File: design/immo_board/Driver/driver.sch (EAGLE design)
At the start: 24 parts, among them IC2 LM393N, IC3 74LS241N

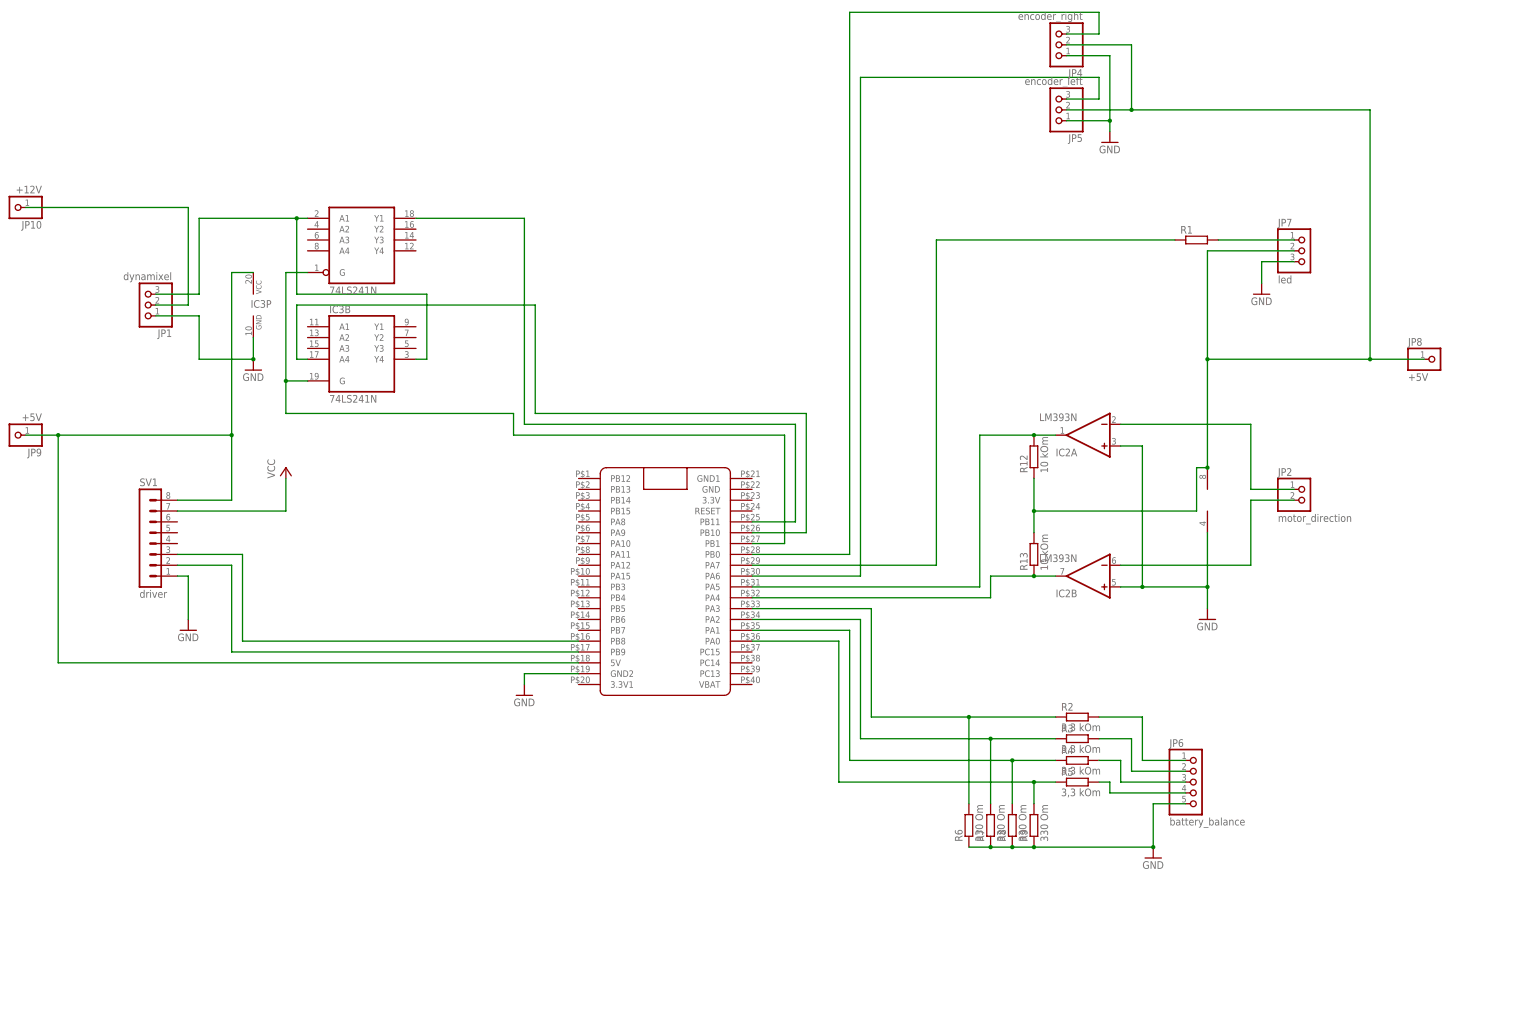
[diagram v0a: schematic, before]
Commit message: Add board for driver. Fix electric scheme.
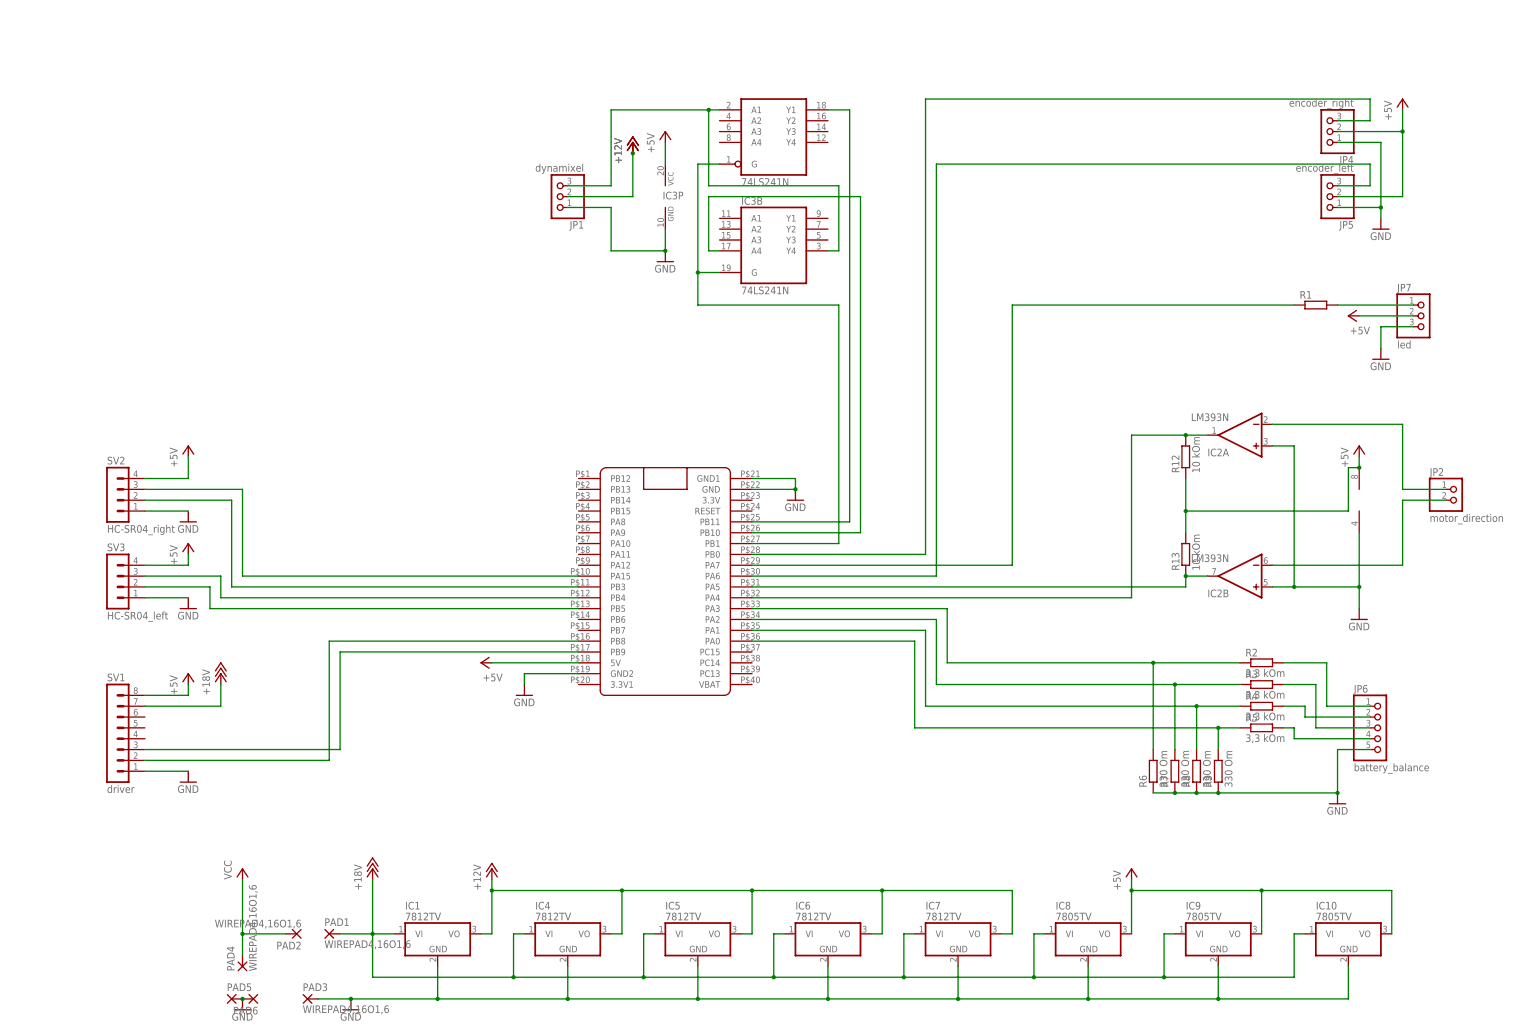
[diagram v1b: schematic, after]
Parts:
- removed JP10: +12V, pinhead:PINHD-1X1
- removed JP8, JP9: +5V, pinhead:PINHD-1X1
- added IC1, IC4, IC5, IC6, IC7: 7812TV, linear:7812TV
- added IC10, IC8, IC9: 7805TV, linear:7805TV
- added PAD1, PAD2, PAD3, PAD4: WIREPAD4,16O1,6, wirepad:WIREPAD4,16O1,6
- added PAD5, PAD6: (no value), wirepad:2,54/1,0
- added SV2: HC-SR04_right, con-lstb:MA04-1
- added SV3: HC-SR04_left, con-lstb:MA04-1
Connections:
- removed net N$24: JP1.2, JP10.1
- new net +12V: IC1.VO, IC4.VO, IC5.VO, IC6.VO, IC7.VO, JP1.2
- new net +18V: IC1.VI, IC10.VI, IC4.VI, IC5.VI, IC6.VI, IC7.VI, IC8.VI, IC9.VI, PAD1.P, SV1.7
- new net +5V: IC10.VO, IC2P.V+, IC3P.VCC, IC8.VO, IC9.VO, JP4.2, JP5.2, JP7.2, R12.1, R13.2, SV1.8, SV2.4, SV3.4, U$1.5V
- new net N$28: SV2.3, U$1.PA15
- new net N$29: SV2.2, U$1.PB3
- net GND: now also IC1.GND, IC10.GND, IC4.GND, IC5.GND, IC6.GND, IC7.GND, IC8.GND, IC9.GND, PAD3.P, PAD5.P, PAD6.P, SV2.1, SV3.1, U$1.GND, U$1.GND1
- net N$14: now also U$1.PA5; no longer U$1.PA4
- net N$20: now also SV1.3; no longer SV1.2
- net N$21: now also SV1.2; no longer SV1.3
- net N$23: now also SV3.2, U$1.PB5; no longer IC2P.V+, JP4.2, JP5.2, JP7.2, JP8.1, R12.1, R13.2
- net N$25: now also SV3.3, U$1.PB4; no longer IC3P.VCC, JP9.1, SV1.8, U$1.5V
- net N$6: now also JP6.2; no longer JP6.3
- net N$7: now also JP6.3; no longer JP6.2
- net N$9: now also U$1.PA4; no longer U$1.PA5
- net VCC: now also PAD2.P, PAD4.P; no longer SV1.7
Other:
- moved on the sheet: IC2A, IC2B, IC3B, IC3P, JP1, JP2, JP4, JP5, JP6, JP7, R1, R12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

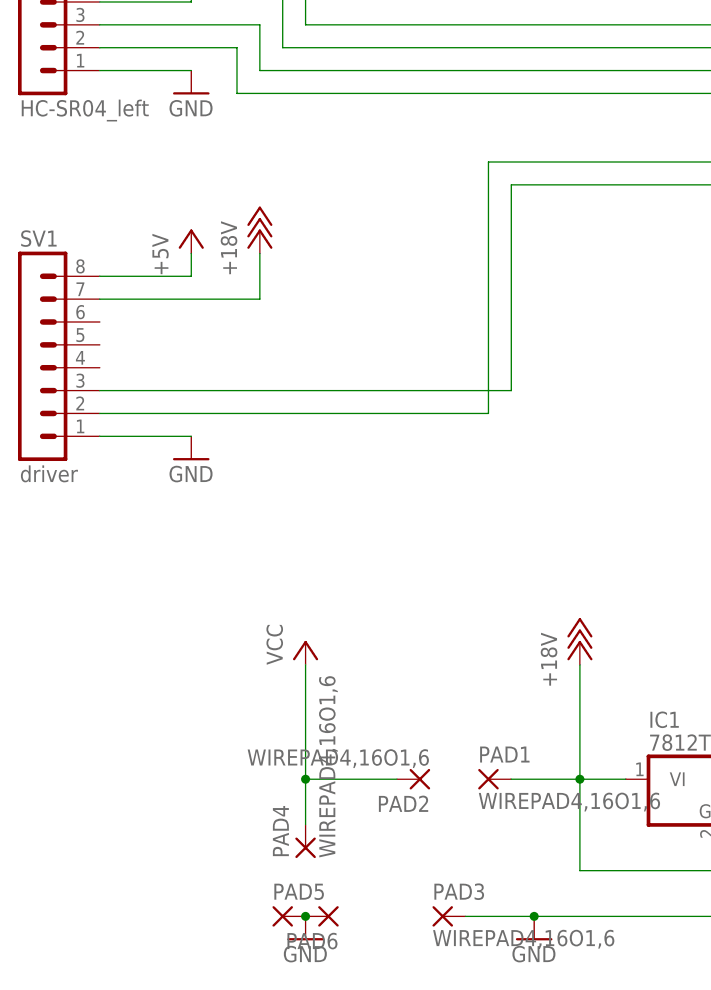
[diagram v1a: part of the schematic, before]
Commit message: Fix board for driver. Fix electric scheme.
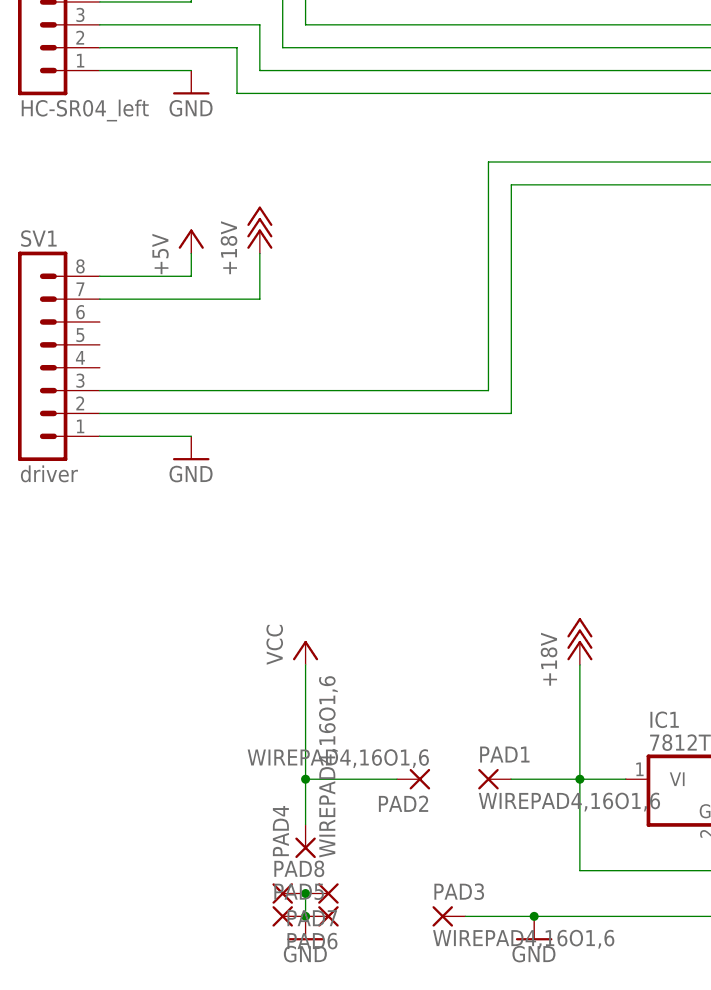
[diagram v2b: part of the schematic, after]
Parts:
- added PAD7, PAD8: (no value), wirepad:2,54/1,0
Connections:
- net GND: now also PAD7.P, PAD8.P
- net N$20: now also SV1.2; no longer SV1.3
- net N$21: now also SV1.3; no longer SV1.2
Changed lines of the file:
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@@
 <part name="PAD6" library="wirepad" deviceset="2,54/1,0" device=""/>
 <part name="GND12" library="supply1" deviceset="GND" device=""/>
+<part name="PAD7" library="wirepad" deviceset="2,54/1,0" device=""/>
+<part name="PAD8" library="wirepad" deviceset="2,54/1,0" device=""/>
 </parts>
 <sheets>
@@
 <instance part="PAD6" gate="P" x="5.08" y="-91.44" rot="R180"/>
 <instance part="GND12" gate="1" x="2.54" y="-93.98"/>
+<instance part="PAD7" gate="P" x="5.08" y="-88.9" rot="R180"/>
+<instance part="PAD8" gate="P" x="0" y="-88.9"/>
 </instances>
 <busses>
@@
 <pinref part="GND12" gate="1" pin="GND"/>
 <junction x="2.54" y="-91.44"/>
-<pinref part="GND12" gate="1" pin="GND"/>
+<pinref part="PAD7" gate="P" pin="P"/>
+<pinref part="PAD8" gate="P" pin="P"/>
+<wire x1="2.54" y1="-91.44" x2="2.54" y2="-88.9" width="0.1524" layer="91"/>
+<junction x="2.54" y="-88.9"/>
 </segment>
 </net>
@@
 <pinref part="U$1" gate="G$1" pin="PB9"/>
 <wire x1="25.4" y1="-10.16" x2="81.28" y2="-10.16" width="0.1524" layer="91"/>
-<wire x1="25.4" y1="-10.16" x2="25.4" y2="-33.02" width="0.1524" layer="91"/>
-<pinref part="SV1" gate="1" pin="3"/>
-<wire x1="25.4" y1="-33.02" x2="-20.32" y2="-33.02" width="0.1524" layer="91"/>
+<wire x1="25.4" y1="-10.16" x2="25.4" y2="-35.56" width="0.1524" layer="91"/>
+<pinref part="SV1" gate="1" pin="2"/>
+<wire x1="-20.32" y1="-35.56" x2="25.4" y2="-35.56" width="0.1524" layer="91"/>
 </segment>
 </net>
@@
 <pinref part="U$1" gate="G$1" pin="PB8"/>
 <wire x1="81.28" y1="-7.62" x2="22.86" y2="-7.62" width="0.1524" layer="91"/>
-<wire x1="22.86" y1="-7.62" x2="22.86" y2="-35.56" width="0.1524" layer="91"/>
-<pinref part="SV1" gate="1" pin="2"/>
-<wire x1="-20.32" y1="-35.56" x2="22.86" y2="-35.56" width="0.1524" layer="91"/>
-</segment>
-</net>
+<wire x1="22.86" y1="-7.62" x2="22.86" y2="-33.02" width="0.1524" layer="91"/>
+<pinref part="SV1" gate="1" pin="3"/>
+<wire x1="22.86" y1="-33.02" x2="-20.32" y2="-33.02" width="0.1524" layer="91"/>
+</segment>
+</net>

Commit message: Fix board and electrical scheme for Encoder, Driver, WS2812B.
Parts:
- removed PAD5, PAD6, PAD7, PAD8: (no value), wirepad:2,54/1,0
- R1: value (none) -> 330 Om
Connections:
- net N$1 renamed P$27
- net N$10 renamed P$36
- net N$11 renamed P$35
- net N$12 renamed P$34
- net N$13 renamed P$33
- net N$14 renamed P$31
- net N$15 renamed P$30
- net N$18 renamed P$29
- net N$20 renamed P$17
- net N$21 renamed P$16
- net N$22 renamed P$28
- net N$23 renamed P$13
- net N$25 renamed P$12
- net N$28 renamed P$10
- net N$29 renamed P$11
- net N$3 renamed P$25
- net N$4 renamed P$26
- net N$9 renamed P$32
- net GND: no longer PAD5.P, PAD6.P, PAD7.P, PAD8.P

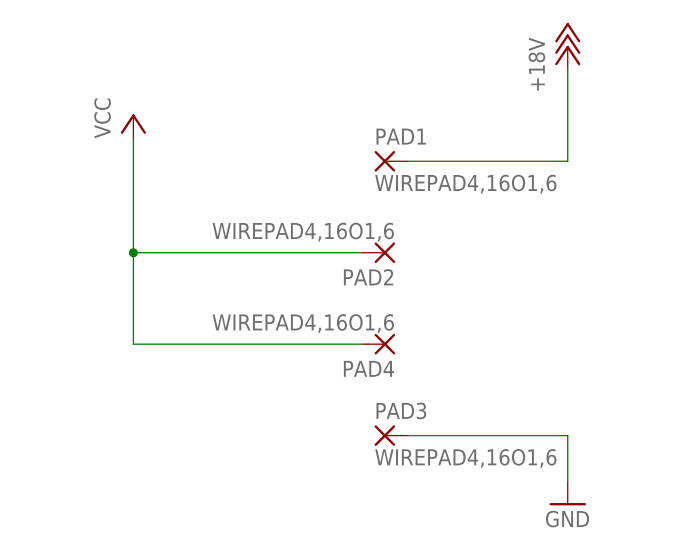
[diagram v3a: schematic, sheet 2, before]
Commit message: Fix board and electric scheme. Add capacitors.
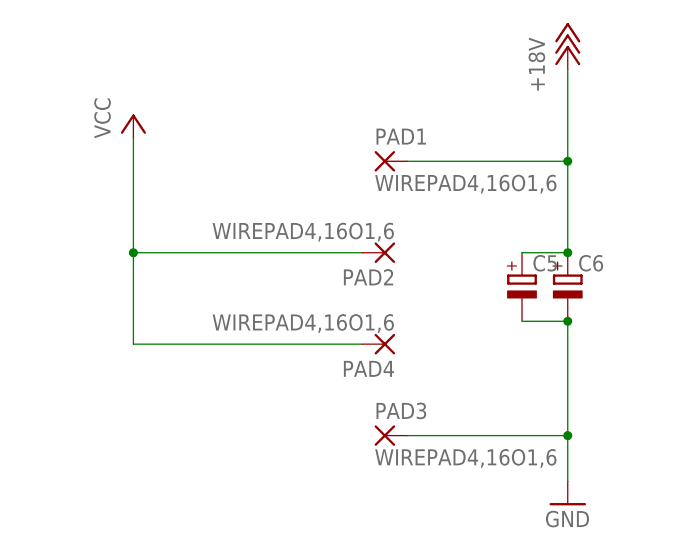
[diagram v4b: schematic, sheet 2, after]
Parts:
- added C1, C4, C5: (no value), resistor:CPOL-EUE5-8.5
- added C2, C3, C6: (no value), resistor:CPOL-EUE2.5-5
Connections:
- net +12V: now also C1.+, C2.+
- net +18V: now also C5.+, C6.+
- net +5V: now also C3.+, C4.+
- net GND: now also C1.-, C2.-, C3.-, C4.-, C5.-, C6.-
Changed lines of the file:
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@@
 <part name="P+17" library="supply1" deviceset="+18V" device=""/>
 <part name="GND14" library="supply1" deviceset="GND" device=""/>
+<part name="C1" library="resistor" deviceset="CPOL-EU" device="E5-8.5"/>
+<part name="C2" library="resistor" deviceset="CPOL-EU" device="E2.5-5"/>
+<part name="C3" library="resistor" deviceset="CPOL-EU" device="E2.5-5"/>
+<part name="C4" library="resistor" deviceset="CPOL-EU" device="E5-8.5"/>
+<part name="C5" library="resistor" deviceset="CPOL-EU" device="E5-8.5"/>
+<part name="C6" library="resistor" deviceset="CPOL-EU" device="E2.5-5"/>
 </parts>
 <sheets>
@@
 <instance part="P+17" gate="1" x="60.96" y="30.48"/>
 <instance part="GND14" gate="1" x="60.96" y="-20.32"/>
+<instance part="C5" gate="G$1" x="55.88" y="5.08"/>
+<instance part="C6" gate="G$1" x="60.96" y="5.08"/>
 </instances>
 <busses>
@@
 <pinref part="PAD3" gate="G$1" pin="P"/>
 <wire x1="43.18" y1="-12.7" x2="60.96" y2="-12.7" width="0.1524" layer="91"/>
+<pinref part="C6" gate="G$1" pin="-"/>
+<wire x1="60.96" y1="-12.7" x2="60.96" y2="0" width="0.1524" layer="91"/>
+<junction x="60.96" y="-12.7"/>
+<pinref part="C5" gate="G$1" pin="-"/>
+<wire x1="60.96" y1="0" x2="55.88" y2="0" width="0.1524" layer="91"/>
+<junction x="60.96" y="0"/>
 </segment>
 </net>
@@
 <wire x1="43.18" y1="17.78" x2="60.96" y2="17.78" width="0.1524" layer="91"/>
 <wire x1="60.96" y1="17.78" x2="60.96" y2="27.94" width="0.1524" layer="91"/>
+<pinref part="C5" gate="G$1" pin="+"/>
+<pinref part="C6" gate="G$1" pin="+"/>
+<wire x1="55.88" y1="7.62" x2="60.96" y2="7.62" width="0.1524" layer="91"/>
+<wire x1="60.96" y1="7.62" x2="60.96" y2="17.78" width="0.1524" layer="91"/>
+<junction x="60.96" y="7.62"/>
+<junction x="60.96" y="17.78"/>
 </segment>
 </net>
@@
 <instance part="P+4" gate="1" x="-10.16" y="71.12"/>
 <instance part="P+6" gate="1" x="17.78" y="71.12"/>
+<instance part="C1" gate="G$1" x="139.7" y="45.72"/>
+<instance part="C2" gate="G$1" x="134.62" y="45.72"/>
 </instances>
 <busses>
@@
 <junction x="96.52" y="40.64"/>
 <pinref part="GND8" gate="1" pin="GND"/>
+<pinref part="C2" gate="G$1" pin="-"/>
+<wire x1="127" y1="40.64" x2="134.62" y2="40.64" width="0.1524" layer="91"/>
+<junction x="127" y="40.64"/>
+<pinref part="C1" gate="G$1" pin="-"/>
+<wire x1="134.62" y1="40.64" x2="139.7" y2="40.64" width="0.1524" layer="91"/>
+<junction x="134.62" y="40.64"/>
 </segment>
 </net>
@@
 <wire x1="17.78" y1="66.04" x2="17.78" y2="68.58" width="0.1524" layer="91"/>
 <junction x="17.78" y="66.04"/>
+<pinref part="C2" gate="G$1" pin="+"/>
+<pinref part="C1" gate="G$1" pin="+"/>
+<wire x1="134.62" y1="48.26" x2="139.7" y2="48.26" width="0.1524" layer="91"/>
+<wire x1="139.7" y1="48.26" x2="139.7" y2="55.88" width="0.1524" layer="91"/>
+<junction x="139.7" y="48.26"/>
+<junction x="139.7" y="55.88"/>
 </segment>
 </net>
@@
 <instance part="P+16" gate="1" x="-2.54" y="58.42"/>
 <instance part="GND13" gate="1" x="-2.54" y="27.94"/>
+<instance part="C3" gate="G$1" x="78.74" y="35.56"/>
+<instance part="C4" gate="G$1" x="83.82" y="35.56"/>
 </instances>
 <busses>
@@
 <wire x1="-2.54" y1="30.48" x2="12.7" y2="30.48" width="0.1524" layer="91"/>
 <junction x="12.7" y="30.48"/>
+<pinref part="C4" gate="G$1" pin="-"/>
+<pinref part="C3" gate="G$1" pin="-"/>
+<wire x1="83.82" y1="30.48" x2="78.74" y2="30.48" width="0.1524" layer="91"/>
+<wire x1="78.74" y1="30.48" x2="73.66" y2="30.48" width="0.1524" layer="91"/>
+<junction x="78.74" y="30.48"/>
+<junction x="73.66" y="30.48"/>
 </segment>
 </net>
@@
 <wire x1="22.86" y1="55.88" x2="22.86" y2="58.42" width="0.1524" layer="91"/>
 <junction x="22.86" y="55.88"/>
-</segment>
-</net>
+<pinref part="C3" gate="G$1" pin="+"/>
+<pinref part="C4" gate="G$1" pin="+"/>
+<wire x1="78.74" y1="38.1" x2="83.82" y2="38.1" width="0.1524" layer="91"/>
+<wire x1="83.82" y1="38.1" x2="83.82" y2="45.72" width="0.1524" layer="91"/>
+<junction x="83.82" y="38.1"/>
+<junction x="83.82" y="45.72"/>
+</segment>
+</net>
